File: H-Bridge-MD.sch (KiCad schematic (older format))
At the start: 70 parts, among them IC1 SI8650AB-B-IS1, IC2 AP7381-50SA-7, IC3 A3921KLPTR-T, IC4 SI8650AB-B-IS1, IC5 A3921KLPTR-T, J1 Conn_01x03, J2 Conn_01x05, J3 Bus_mechaken_PCIexpress_x16_1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, J4 Conn_01x02, J5 Conn_01x02, Q1 NVMFD5C446NT1G, Q2 NVMFD5C446NT1G, Q3 NVMFD5C446NT1G, Q4 NVMFD5C446NT1G, U1 LDL1117S33R_SOT223-4, U2 STM32F042K6Tx, U3 MCP2562-E-SN

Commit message: fix
細かな修正
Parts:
- IC2: footprint SamacSys_Parts:SOT96P240X105-3N -> SOT96P240X105-3N; symbol SamacSys_Parts:AP7381-50SA-7 -> H-Bridge-MD-rescue:AP7381-50SA-7-SamacSys_Parts
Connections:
- net MD_3V3 renamed VDD
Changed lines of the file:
@@
 Text GLabel 7600 8550 3    50   Input ~ 0
 MD_FF2_1
-Text GLabel 12750 4150 0    50   Output ~ 0
-MD_3V3
 Text Label 4800 3600 0    50   ~ 0
 CAN_TD
@@
 	0    -1   -1   0
 $EndComp
-Text GLabel 10250 3900 2    50   Input ~ 0
-MD_3V3
-Text GLabel 6050 7450 2    50   Input ~ 0
-MD_3V3
 Connection ~ 9850 10100
 Wire Wire Line
@@
 	1    0    0    -1
 $EndComp
-Text GLabel 11200 4100 3    50   Output ~ 0
-MD_3V3
 Text GLabel 11050 5100 1    50   Input ~ 0
 VREG_0
@@
 Connection ~ 11850 5000
 $Comp
-L SamacSys_Parts:AP7381-50SA-7 IC2
+L H-Bridge-MD-rescue:AP7381-50SA-7-SamacSys_Parts IC2
 U 1 1 5E271866
 P 13300 4050
 F 0 "IC2" H 13850 4315 50  0000 C CNN
 F 1 "AP7381-50SA-7" H 13850 4224 50  0000 C CNN
-F 2 "SamacSys_Parts:SOT96P240X105-3N" H 14250 4150 50  0001 L CNN
+F 2 "SOT96P240X105-3N" H 14250 4150 50  0001 L CNN
 F 3 "https://componentsearchengine.com/Datasheets/1/AP7381-50SA-7.pdf" H 14250 4050 50  0001 L CNN
 F 4 "LDO Voltage Regulators LDO CMOS LowCurr SOT23 T&R 3K" H 14250 3950 50  0001 L CNN "Description"
@@
 Wire Wire Line
 	13100 4450 14400 4450
-Wire Wire Line
-	14400 4450 14400 4050
 Connection ~ 14400 4450
+Wire Wire Line
+	14400 4050 14400 4450
+$Comp
+L power:VDD #PWR0101
+U 1 1 5E33BBA2
+P 11200 4100
+F 0 "#PWR0101" H 11200 3950 50  0001 C CNN
+F 1 "VDD" H 11217 4273 50  0000 C CNN
+F 2 "" H 11200 4100 50  0001 C CNN
+F 3 "" H 11200 4100 50  0001 C CNN
+	1    11200 4100
+	-1   0    0    1
+$EndComp
+$Comp
+L power:VDD #PWR0102
+U 1 1 5E35E290
+P 12750 4150
+F 0 "#PWR0102" H 12750 4000 50  0001 C CNN
+F 1 "VDD" H 12767 4323 50  0000 C CNN
+F 2 "" H 12750 4150 50  0001 C CNN
+F 3 "" H 12750 4150 50  0001 C CNN
+	1    12750 4150
+	0    -1   -1   0
+$EndComp
+$Comp
+L power:VDD #PWR0103
+U 1 1 5E3654B8
+P 10250 3900
+F 0 "#PWR0103" H 10250 3750 50  0001 C CNN
+F 1 "VDD" H 10267 4073 50  0000 C CNN
+F 2 "" H 10250 3900 50  0001 C CNN
+F 3 "" H 10250 3900 50  0001 C CNN
+	1    10250 3900
+	1    0    0    -1
+$EndComp
+$Comp
+L power:VDD #PWR0104
+U 1 1 5E36C54F
+P 6050 7450
+F 0 "#PWR0104" H 6050 7300 50  0001 C CNN
+F 1 "VDD" H 6067 7623 50  0000 C CNN
+F 2 "" H 6050 7450 50  0001 C CNN
+F 3 "" H 6050 7450 50  0001 C CNN
+	1    6050 7450
+	1    0    0    -1
+$EndComp
 $EndSCHEMATC

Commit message: clean
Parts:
- removed IC2: AP7381-50SA-7, SOT96P240X105-3N, symbol H-Bridge-MD-rescue:AP7381-50SA-7-SamacSys_Parts
- added IC2: AP7381-50SA-7, SOT96P240X105-3N, symbol SamacSys_Parts:AP7381-50SA-7
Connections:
- net GNDPWR: now also IC2.3 (GND)
- net VCC: now also IC2.1 (VIN)
- net VDD renamed MD_3V3
- net MD_3V3: now also IC2.2 (VOUT)
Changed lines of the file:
@@
 Text GLabel 7600 8550 3    50   Input ~ 0
 MD_FF2_1
+Text GLabel 12750 4150 0    50   Output ~ 0
+MD_3V3
 Text Label 4800 3600 0    50   ~ 0
 CAN_TD
@@
 	0    -1   -1   0
 $EndComp
+Text GLabel 10250 3900 2    50   Input ~ 0
+MD_3V3
+Text GLabel 6050 7450 2    50   Input ~ 0
+MD_3V3
 Connection ~ 9850 10100
 Wire Wire Line
@@
 F 3 "" H 12000 4050 50  0001 C CNN
 	1    12000 4100
-	1    0    0    -1
-$EndComp
-$Comp
-L power:PWR_FLAG #FLG04
-U 1 1 5E1278AA
-P 11200 4100
-F 0 "#FLG04" H 11200 4175 50  0001 C CNN
-F 1 "PWR_FLAG" H 11200 4273 50  0000 C CNN
-F 2 "" H 11200 4100 50  0001 C CNN
-F 3 "~" H 11200 4100 50  0001 C CNN
-	1    11200 4100
 	1    0    0    -1
 $EndComp
@@
 Connection ~ 11850 5000
 $Comp
-L H-Bridge-MD-rescue:AP7381-50SA-7-SamacSys_Parts IC2
-U 1 1 5E271866
+L Device:C C5
+U 1 1 5DF18189
+P 13100 4200
+F 0 "C5" H 13215 4246 50  0000 L CNN
+F 1 "1u" H 13215 4155 50  0000 L CNN
+F 2 "Capacitor_SMD:C_0805_2012Metric" H 13138 4050 50  0001 C CNN
+F 3 "~" H 13100 4200 50  0001 C CNN
+	1    13100 4200
+	1    0    0    -1
+$EndComp
+Wire Wire Line
+	13300 4050 13100 4050
+Connection ~ 13100 4050
+Wire Wire Line
+	13100 4050 13000 4050
+Wire Wire Line
+	12750 4150 12800 4150
+Connection ~ 12800 4150
+Wire Wire Line
+	12800 4150 13300 4150
+Wire Wire Line
+	12800 4450 13100 4450
+Wire Wire Line
+	13100 4350 13100 4450
+Connection ~ 13100 4450
+Wire Wire Line
+	13100 4450 14400 4450
+Wire Wire Line
+	14400 4450 14400 4050
+Connection ~ 14400 4450
+$Comp
+L SamacSys_Parts:AP7381-50SA-7 IC2
+U 1 1 5E358498
 P 13300 4050
 F 0 "IC2" H 13850 4315 50  0000 C CNN
@@
 	1    0    0    -1
 $EndComp
-$Comp
-L Device:C C5
-U 1 1 5DF18189
-P 13100 4200
-F 0 "C5" H 13215 4246 50  0000 L CNN
-F 1 "1u" H 13215 4155 50  0000 L CNN
-F 2 "Capacitor_SMD:C_0805_2012Metric" H 13138 4050 50  0001 C CNN
-F 3 "~" H 13100 4200 50  0001 C CNN
-	1    13100 4200
-	1    0    0    -1
-$EndComp
-Wire Wire Line
-	13300 4050 13100 4050
-Connection ~ 13100 4050
-Wire Wire Line
-	13100 4050 13000 4050
-Wire Wire Line
-	12750 4150 12800 4150
-Connection ~ 12800 4150
-Wire Wire Line
-	12800 4150 13300 4150
-Wire Wire Line
-	12800 4450 13100 4450
-Wire Wire Line
-	13100 4350 13100 4450
-Connection ~ 13100 4450
-Wire Wire Line
-	13100 4450 14400 4450
-Connection ~ 14400 4450
-Wire Wire Line
-	14400 4050 14400 4450
-$Comp
-L power:VDD #PWR0101
-U 1 1 5E33BBA2
-P 11200 4100
-F 0 "#PWR0101" H 11200 3950 50  0001 C CNN
-F 1 "VDD" H 11217 4273 50  0000 C CNN
-F 2 "" H 11200 4100 50  0001 C CNN
-F 3 "" H 11200 4100 50  0001 C CNN
-	1    11200 4100
-	-1   0    0    1
-$EndComp
-$Comp
-L power:VDD #PWR0102
-U 1 1 5E35E290
-P 12750 4150
-F 0 "#PWR0102" H 12750 4000 50  0001 C CNN
-F 1 "VDD" H 12767 4323 50  0000 C CNN
-F 2 "" H 12750 4150 50  0001 C CNN
-F 3 "" H 12750 4150 50  0001 C CNN
-	1    12750 4150
-	0    -1   -1   0
-$EndComp
-$Comp
-L power:VDD #PWR0103
-U 1 1 5E3654B8
-P 10250 3900
-F 0 "#PWR0103" H 10250 3750 50  0001 C CNN
-F 1 "VDD" H 10267 4073 50  0000 C CNN
-F 2 "" H 10250 3900 50  0001 C CNN
-F 3 "" H 10250 3900 50  0001 C CNN
-	1    10250 3900
-	1    0    0    -1
-$EndComp
-$Comp
-L power:VDD #PWR0104
-U 1 1 5E36C54F
-P 6050 7450
-F 0 "#PWR0104" H 6050 7300 50  0001 C CNN
-F 1 "VDD" H 6067 7623 50  0000 C CNN
-F 2 "" H 6050 7450 50  0001 C CNN
-F 3 "" H 6050 7450 50  0001 C CNN
-	1    6050 7450
-	1    0    0    -1
-$EndComp

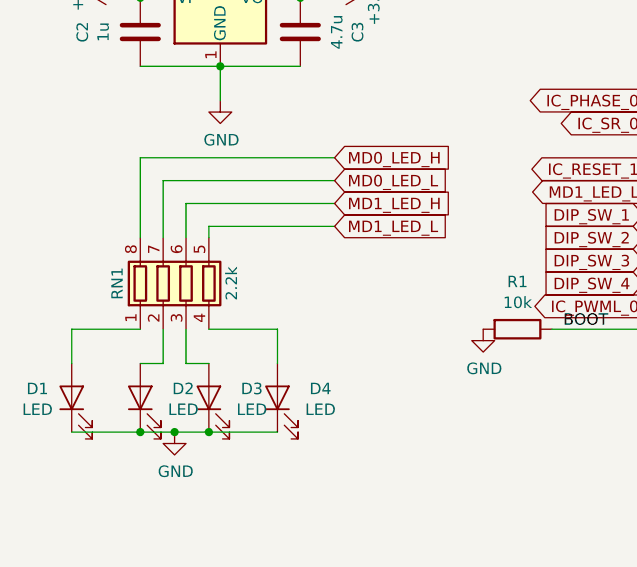
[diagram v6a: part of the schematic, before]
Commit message: change
check to elecrow
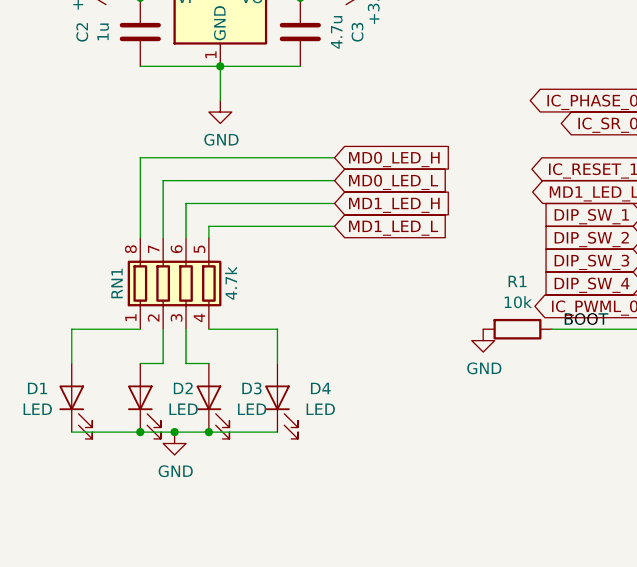
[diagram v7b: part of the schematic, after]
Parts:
- RN1: value 2.2k -> 4.7k
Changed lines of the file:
@@
 	7300 9900 7300 9800
-$Comp
-L Device:R R13
-U 1 1 5DA97C08
-P 2000 9600
-F 0 "R13" V 1793 9600 50  0000 C CNN
-F 1 "21" V 1884 9600 50  0000 C CNN
-F 2 "Resistor_SMD:R_0603_1608Metric" V 1930 9600 50  0001 C CNN
-F 3 "~" H 2000 9600 50  0001 C CNN
-	1    2000 9600
-	0    1    1    0
-$EndComp
-$Comp
-L Device:R R18
-U 1 1 5DA97BF0
-P 2000 9800
-F 0 "R18" V 1885 9800 50  0000 C CNN
-F 1 "21" V 1794 9800 50  0000 C CNN
-F 2 "Resistor_SMD:R_0603_1608Metric" V 1930 9800 50  0001 C CNN
-F 3 "~" H 2000 9800 50  0001 C CNN
-	1    2000 9800
-	0    -1   -1   0
-$EndComp
 $Comp
 L power:GNDPWR #PWR054
@@
 	1    0    0    -1
 $EndComp
-$Comp
-L Device:R R9
-U 1 1 5DC02421
-P 9350 6550
-F 0 "R9" V 9235 6550 50  0000 C CNN
-F 1 "21" V 9144 6550 50  0000 C CNN
-F 2 "Resistor_SMD:R_0603_1608Metric" V 9280 6550 50  0001 C CNN
-F 3 "~" H 9350 6550 50  0001 C CNN
-	1    9350 6550
-	0    -1   -1   0
-$EndComp
-$Comp
-L Device:R R7
-U 1 1 5DC02427
-P 9350 6350
-F 0 "R7" V 9150 6350 50  0000 C CNN
-F 1 "21" V 9250 6350 50  0000 C CNN
-F 2 "Resistor_SMD:R_0603_1608Metric" V 9280 6350 50  0001 C CNN
-F 3 "~" H 9350 6350 50  0001 C CNN
-	1    9350 6350
-	0    1    1    0
-$EndComp
 Text GLabel 9200 6550 0    50   Input ~ 0
 GHB_0
@@
 Text GLabel 6650 6600 0    50   Input ~ 0
 GLB_0
-$Comp
-L Device:R R10
-U 1 1 5DC02488
-P 6800 6600
-F 0 "R10" V 6915 6600 50  0000 C CNN
-F 1 "21" V 7006 6600 50  0000 C CNN
-F 2 "Resistor_SMD:R_0603_1608Metric" V 6730 6600 50  0001 C CNN
-F 3 "~" H 6800 6600 50  0001 C CNN
-	1    6800 6600
-	0    1    1    0
-$EndComp
 $Comp
 L power:GNDPWR #PWR043
@@
 P 1200 2900
 F 0 "RN1" V 900 2900 50  0000 C CNN
-F 1 "2.2k" V 1400 2900 50  0000 C CNN
+F 1 "4.7k" V 1400 2900 50  0000 C CNN
 F 2 "Resistor_SMD:R_Array_Convex_4x1206" V 1475 2900 50  0001 C CNN
 F 3 "~" H 1200 2900 50  0001 C CNN
@@
 	1    6950 6250
 	1    0    0    -1
-$EndComp
-$Comp
-L Device:R R8
-U 1 1 5DC0241B
-P 6800 6400
-F 0 "R8" V 7007 6400 50  0000 C CNN
-F 1 "21" V 6916 6400 50  0000 C CNN
-F 2 "Resistor_SMD:R_0603_1608Metric" V 6730 6400 50  0001 C CNN
-F 3 "~" H 6800 6400 50  0001 C CNN
-	1    6800 6400
-	0    -1   -1   0
 $EndComp
 $Comp
@@
 Text GLabel 6300 1900 0    50   Output ~ 0
 DIP_SW_4
-$Comp
-L Device:R R14
-U 1 1 5DA97C02
-P 5000 9600
-F 0 "R14" V 4750 9600 50  0000 C CNN
-F 1 "21" V 4850 9600 50  0000 C CNN
-F 2 "Resistor_SMD:R_0603_1608Metric" V 4930 9600 50  0001 C CNN
-F 3 "~" H 5000 9600 50  0001 C CNN
-	1    5000 9600
-	0    1    1    0
-$EndComp
 Text GLabel 4850 9600 0    50   Input ~ 0
 GLA_1
 Text GLabel 4850 9800 0    50   Input ~ 0
 GLB_1
-$Comp
-L Device:R R19
-U 1 1 5DA97BEA
-P 5000 9800
-F 0 "R19" V 4885 9800 50  0000 C CNN
-F 1 "21" V 4794 9800 50  0000 C CNN
-F 2 "Resistor_SMD:R_0603_1608Metric" V 4930 9800 50  0001 C CNN
-F 3 "~" H 5000 9800 50  0001 C CNN
-	1    5000 9800
-	0    -1   -1   0
-$EndComp
 $Comp
 L Device:C C9
@@
 	1    0    0    -1
 $EndComp
+$Comp
+L Device:R R19
+U 1 1 5DA97BEA
+P 5000 9800
+F 0 "R19" V 4885 9800 50  0000 C CNN
+F 1 "21" V 4794 9800 50  0000 C CNN
+F 2 "Resistor_SMD:R_0603_1608Metric" V 4930 9800 50  0001 C CNN
+F 3 "~" H 5000 9800 50  0001 C CNN
+	1    5000 9800
+	0    -1   -1   0
+$EndComp
+$Comp
+L Device:R R14
+U 1 1 5DA97C02
+P 5000 9600
+F 0 "R14" V 4750 9600 50  0000 C CNN
+F 1 "21" V 4850 9600 50  0000 C CNN
+F 2 "Resistor_SMD:R_0603_1608Metric" V 4930 9600 50  0001 C CNN
+F 3 "~" H 5000 9600 50  0001 C CNN
+	1    5000 9600
+	0    1    1    0
+$EndComp
+$Comp
+L Device:R R18
+U 1 1 5DA97BF0
+P 2000 9800
+F 0 "R18" V 1885 9800 50  0000 C CNN
+F 1 "21" V 1794 9800 50  0000 C CNN
+F 2 "Resistor_SMD:R_0603_1608Metric" V 1930 9800 50  0001 C CNN
+F 3 "~" H 2000 9800 50  0001 C CNN
+	1    2000 9800
+	0    -1   -1   0
+$EndComp
+$Comp
+L Device:R R13
+U 1 1 5DA97C08
+P 2000 9600
+F 0 "R13" V 1793 9600 50  0000 C CNN
+F 1 "21" V 1884 9600 50  0000 C CNN
+F 2 "Resistor_SMD:R_0603_1608Metric" V 1930 9600 50  0001 C CNN
+F 3 "~" H 2000 9600 50  0001 C CNN
+	1    2000 9600
+	0    1    1    0
+$EndComp
+$Comp
+L Device:R R10
+U 1 1 5DC02488
+P 6800 6600
+F 0 "R10" V 6915 6600 50  0000 C CNN
+F 1 "21" V 7006 6600 50  0000 C CNN
+F 2 "Resistor_SMD:R_0603_1608Metric" V 6730 6600 50  0001 C CNN
+F 3 "~" H 6800 6600 50  0001 C CNN
+	1    6800 6600
+	0    1    1    0
+$EndComp
+$Comp
+L Device:R R8
+U 1 1 5DC0241B
+P 6800 6400
+F 0 "R8" V 7007 6400 50  0000 C CNN
+F 1 "21" V 6916 6400 50  0000 C CNN
+F 2 "Resistor_SMD:R_0603_1608Metric" V 6730 6400 50  0001 C CNN
+F 3 "~" H 6800 6400 50  0001 C CNN
+	1    6800 6400
+	0    -1   -1   0
+$EndComp
+$Comp
+L Device:R R9
+U 1 1 5DC02421
+P 9350 6550
+F 0 "R9" V 9235 6550 50  0000 C CNN
+F 1 "21" V 9144 6550 50  0000 C CNN
+F 2 "Resistor_SMD:R_0603_1608Metric" V 9280 6550 50  0001 C CNN
+F 3 "~" H 9350 6550 50  0001 C CNN
+	1    9350 6550
+	0    -1   -1   0
+$EndComp
+$Comp
+L Device:R R7
+U 1 1 5DC02427
+P 9350 6350
+F 0 "R7" V 9150 6350 50  0000 C CNN
+F 1 "21" V 9250 6350 50  0000 C CNN
+F 2 "Resistor_SMD:R_0603_1608Metric" V 9280 6350 50  0001 C CNN
+F 3 "~" H 9350 6350 50  0001 C CNN
+	1    9350 6350
+	0    1    1    0
+$EndComp
 $EndSCHEMATC

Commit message: change
3Dデータを関連付け
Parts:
- IC2: footprint SOT96P240X105-3N -> SamacSys_Parts:SOT96P240X105-3N
- S2: footprint Package_DIP:DIP-8_W7.62mm -> Button_Switch_THT:SW_DIP_SPSTx04_Slide_9.78x12.34mm_W7.62mm_P2.54mm
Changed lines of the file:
@@
 F 0 "S2" H 6469 2165 50  0000 L CNN
 F 1 "DIPSW" H 6469 2074 50  0000 L CNN
-F 2 "Package_DIP:DIP-8_W7.62mm" H 6950 2000 50  0001 L CNN
+F 2 "Button_Switch_THT:SW_DIP_SPSTx04_Slide_9.78x12.34mm_W7.62mm_P2.54mm" H 6950 2000 50  0001 L CNN
 F 3 "http://uk.rs-online.com/web/p/products/8772264" H 6950 1900 50  0001 L CNN
 F 4 "4 Way Surface Mount DIP Switch SPST, Raised Actuator Slide Actuator" H 6950 1800 50  0001 L CNN "Description"
@@
 F 0 "IC2" H 13850 4315 50  0000 C CNN
 F 1 "AP7381-50SA-7" H 13850 4224 50  0000 C CNN
-F 2 "SOT96P240X105-3N" H 14250 4150 50  0001 L CNN
+F 2 "SamacSys_Parts:SOT96P240X105-3N" H 14250 4150 50  0001 L CNN
 F 3 "https://componentsearchengine.com/Datasheets/1/AP7381-50SA-7.pdf" H 14250 4050 50  0001 L CNN
 F 4 "LDO Voltage Regulators LDO CMOS LowCurr SOT23 T&R 3K" H 14250 3950 50  0001 L CNN "Description"
